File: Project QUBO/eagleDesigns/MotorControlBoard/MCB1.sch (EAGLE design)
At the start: 2 parts, among them U1 PCA9685

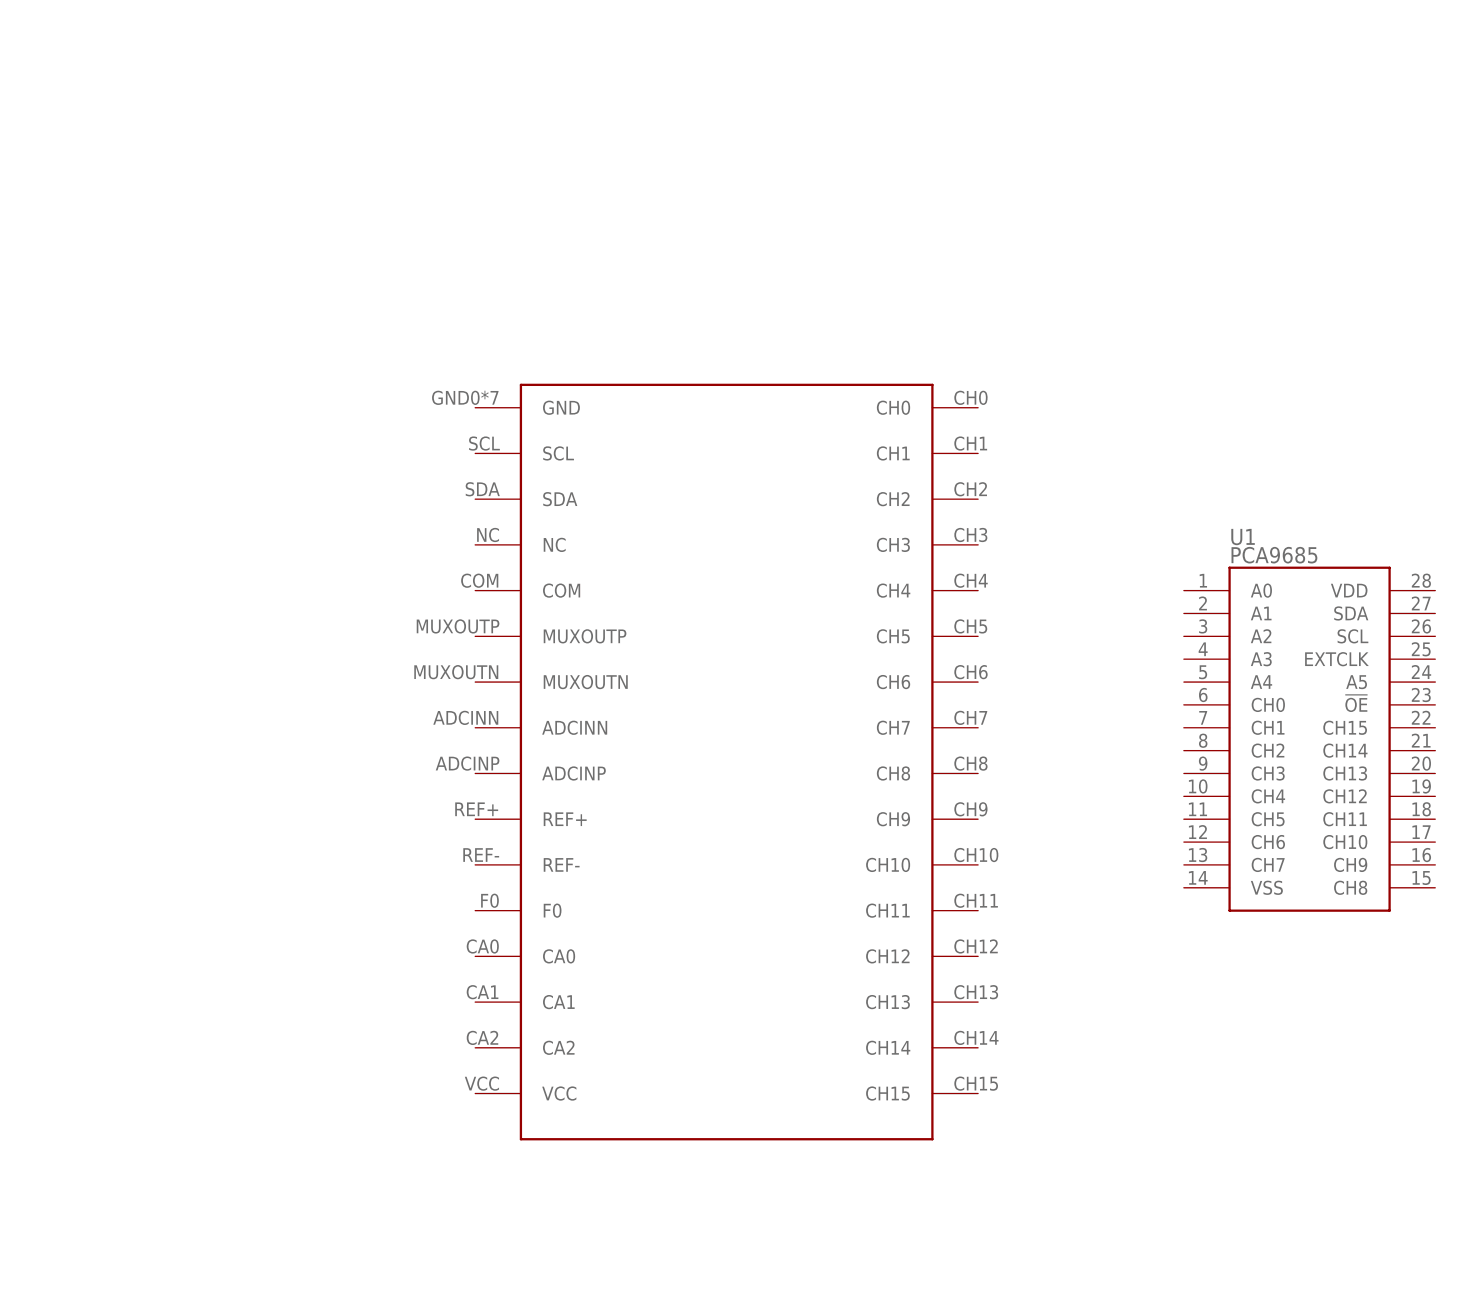
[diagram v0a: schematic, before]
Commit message: 
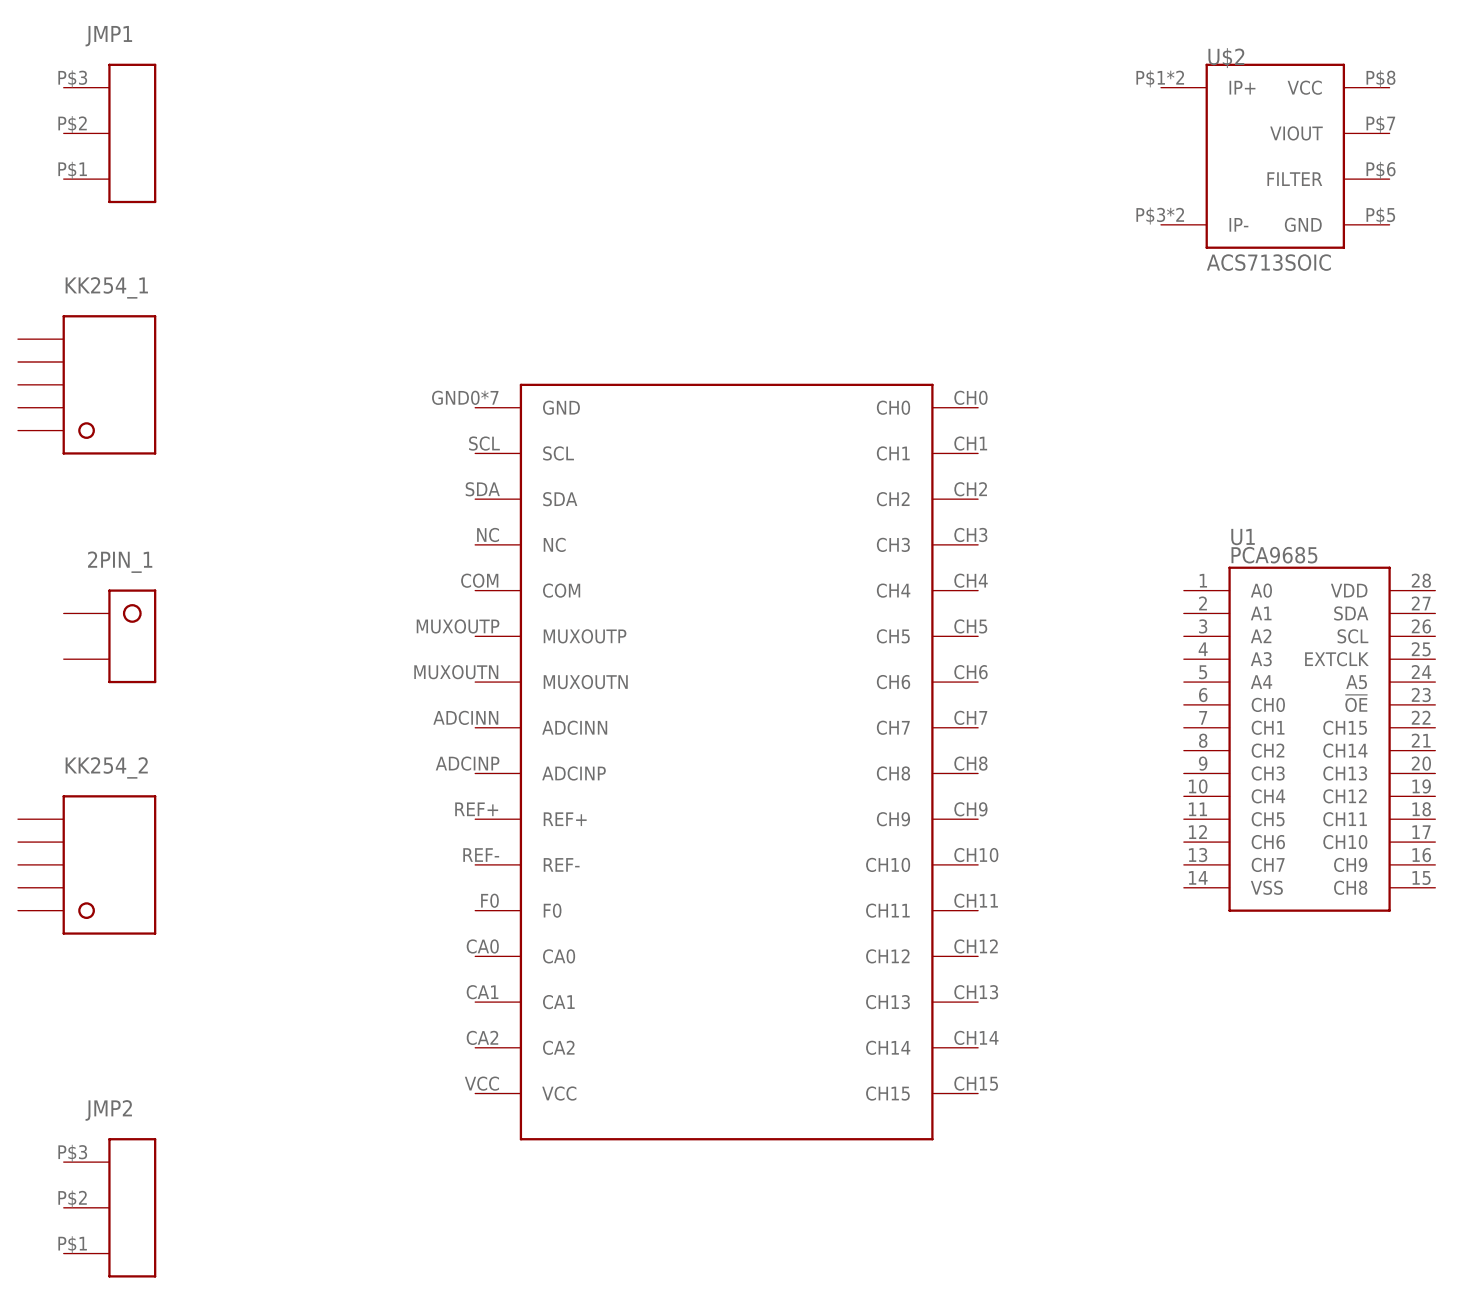
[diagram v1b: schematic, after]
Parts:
- added 2PIN_1: (no value), molex:KK254_VERT_2PIN22-29-2021
- added JMP1, JMP2: (no value), molex:KK254_VERT_3PIN22-10-2031
- added KK254_1, KK254_2: (no value), molex:KK254_VERT_5PIN
- added U$2: ACS713SOIC, allegro:ACS713SOIC
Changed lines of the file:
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@@
 <part name="U1" library="SparkFun-DigitalIC" deviceset="PCA9685" device="" value="PCA9685"/>
 <part name="U$1" library="linear" deviceset="LTC2497" device="UHF"/>
+<part name="U$2" library="allegro" deviceset="ACS713" device="SOIC"/>
+<part name="JMP1" library="molex" deviceset="KK254_VERT_3PIN" device="22-10-2031"/>
+<part name="JMP2" library="molex" deviceset="KK254_VERT_3PIN" device="22-10-2031"/>
+<part name="2PIN_1" library="molex" deviceset="KK254_VERT_2PIN" device="22-29-2021"/>
+<part name="KK254_1" library="molex" deviceset="KK254_VERT_5PIN" device=""/>
+<part name="KK254_2" library="molex" deviceset="KK254_VERT_5PIN" device=""/>
 </parts>
 <sheets>
@@
 <instance part="U1" gate="G$1" x="7.62" y="43.18"/>
 <instance part="U$1" gate="G$1" x="-45.72" y="63.5"/>
+<instance part="U$2" gate="G$1" x="12.7" y="127"/>
+<instance part="JMP1" gate="JMP1" x="-114.3" y="129.54"/>
+<instance part="JMP2" gate="JMP1" x="-114.3" y="10.16"/>
+<instance part="2PIN_1" gate="U1" x="-114.3" y="73.66"/>
+<instance part="KK254_1" gate="G$1" x="-116.84" y="101.6"/>
+<instance part="KK254_2" gate="G$1" x="-116.84" y="48.26"/>
 </instances>
 <busses>

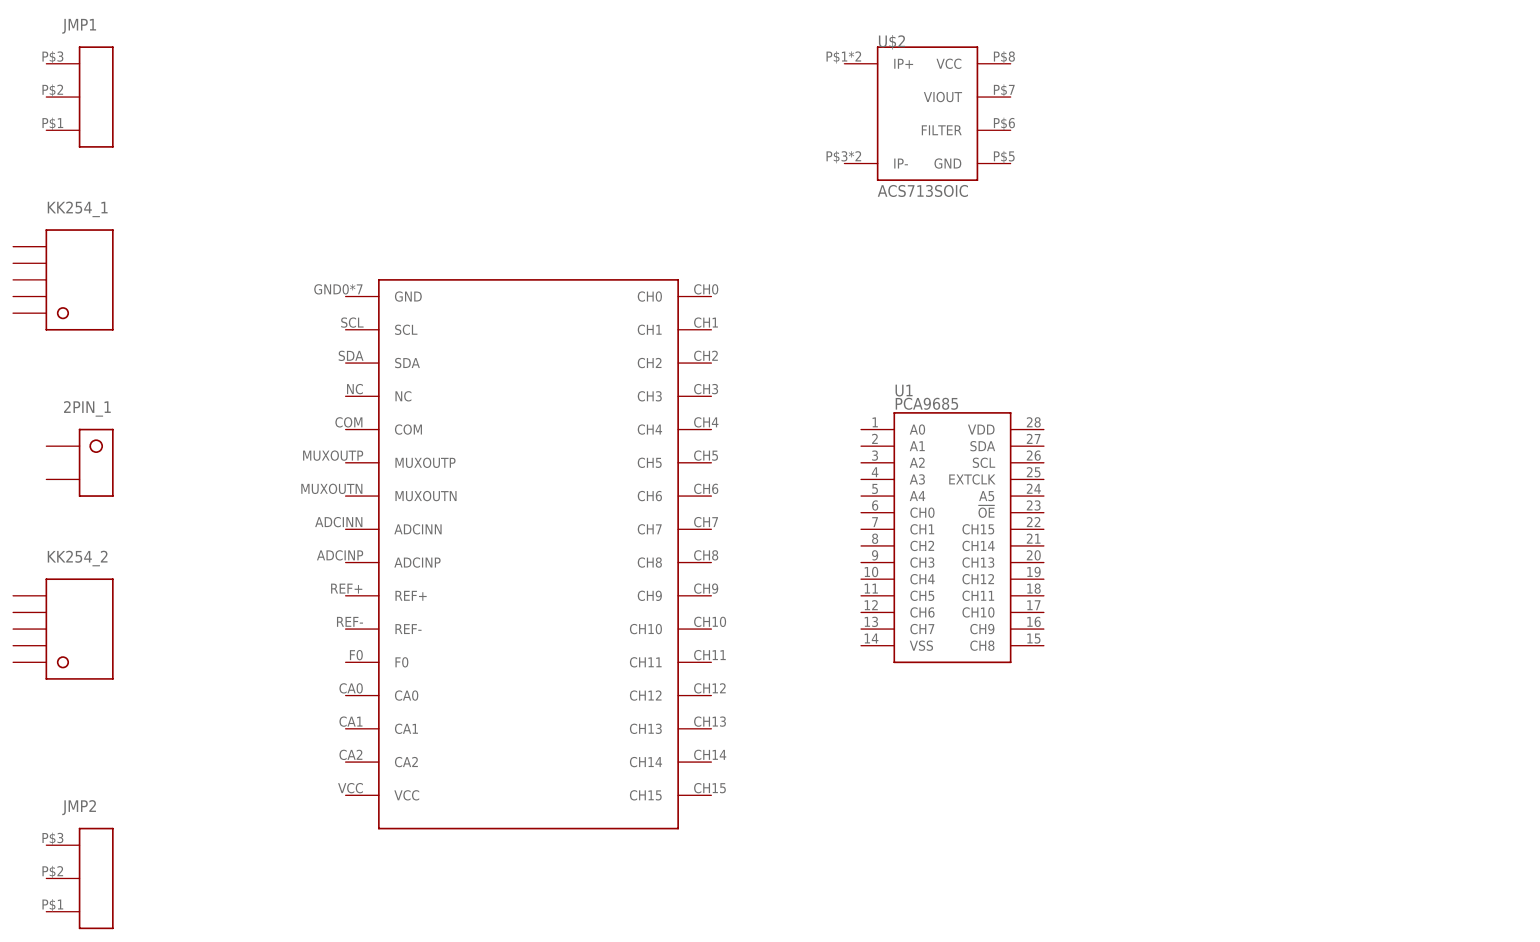
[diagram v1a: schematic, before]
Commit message: 
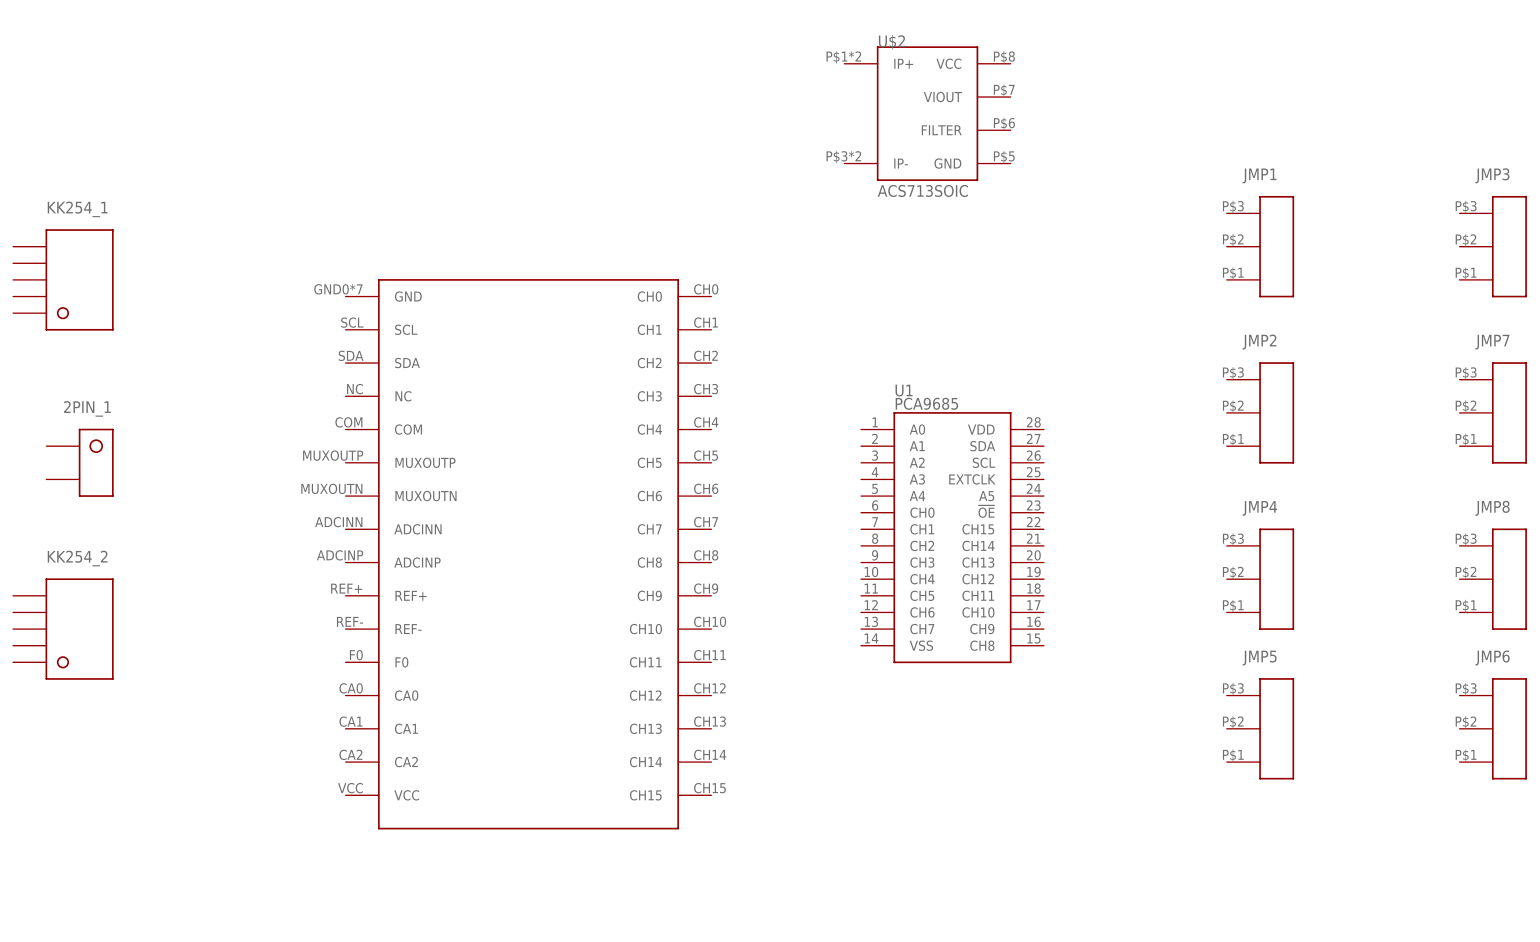
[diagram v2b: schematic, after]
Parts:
- added JMP3, JMP4, JMP5, JMP6, JMP7, JMP8: (no value), molex:KK254_VERT_3PIN22-10-2031
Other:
- moved on the sheet: JMP1, JMP2
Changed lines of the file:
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@@
 <part name="U$1" library="linear" deviceset="LTC2497" device="UHF"/>
 <part name="U$2" library="allegro" deviceset="ACS713" device="SOIC"/>
-<part name="JMP1" library="molex" deviceset="KK254_VERT_3PIN" device="22-10-2031"/>
-<part name="JMP2" library="molex" deviceset="KK254_VERT_3PIN" device="22-10-2031"/>
 <part name="2PIN_1" library="molex" deviceset="KK254_VERT_2PIN" device="22-29-2021"/>
 <part name="KK254_1" library="molex" deviceset="KK254_VERT_5PIN" device=""/>
 <part name="KK254_2" library="molex" deviceset="KK254_VERT_5PIN" device=""/>
+<part name="JMP3" library="molex" deviceset="KK254_VERT_3PIN" device="22-10-2031"/>
+<part name="JMP1" library="molex" deviceset="KK254_VERT_3PIN" device="22-10-2031"/>
+<part name="JMP2" library="molex" deviceset="KK254_VERT_3PIN" device="22-10-2031"/>
+<part name="JMP4" library="molex" deviceset="KK254_VERT_3PIN" device="22-10-2031"/>
+<part name="JMP5" library="molex" deviceset="KK254_VERT_3PIN" device="22-10-2031"/>
+<part name="JMP6" library="molex" deviceset="KK254_VERT_3PIN" device="22-10-2031"/>
+<part name="JMP7" library="molex" deviceset="KK254_VERT_3PIN" device="22-10-2031"/>
+<part name="JMP8" library="molex" deviceset="KK254_VERT_3PIN" device="22-10-2031"/>
 </parts>
 <sheets>
@@
 <instance part="U$1" gate="G$1" x="-45.72" y="63.5"/>
 <instance part="U$2" gate="G$1" x="12.7" y="127"/>
-<instance part="JMP1" gate="JMP1" x="-114.3" y="129.54"/>
-<instance part="JMP2" gate="JMP1" x="-114.3" y="10.16"/>
 <instance part="2PIN_1" gate="U1" x="-114.3" y="73.66"/>
 <instance part="KK254_1" gate="G$1" x="-116.84" y="101.6"/>
 <instance part="KK254_2" gate="G$1" x="-116.84" y="48.26"/>
+<instance part="JMP3" gate="JMP1" x="101.6" y="106.68"/>
+<instance part="JMP1" gate="JMP1" x="66.04" y="106.68"/>
+<instance part="JMP2" gate="JMP1" x="66.04" y="81.28"/>
+<instance part="JMP4" gate="JMP1" x="66.04" y="55.88"/>
+<instance part="JMP5" gate="JMP1" x="66.04" y="33.02"/>
+<instance part="JMP6" gate="JMP1" x="101.6" y="33.02"/>
+<instance part="JMP7" gate="JMP1" x="101.6" y="81.28"/>
+<instance part="JMP8" gate="JMP1" x="101.6" y="55.88"/>
 </instances>
 <busses>
